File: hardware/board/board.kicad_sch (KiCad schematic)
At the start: 64 parts, among them J1 Power, J10 OUT B3, J12 IN C, J13 OUT C1, J14 OUT C2, J15 OUT C3, J17 OUT D, J18 IN D1, J19 IN D2, J2 IN A, J20 IN D3, J3 OUT A1, J4 OUT A2, J5 OUT A3, J7 IN B, J8 OUT B1, J9 OUT B2, U1 OPA4991, U2 OPA4991, U4 OPA4991, U6 OPA4991

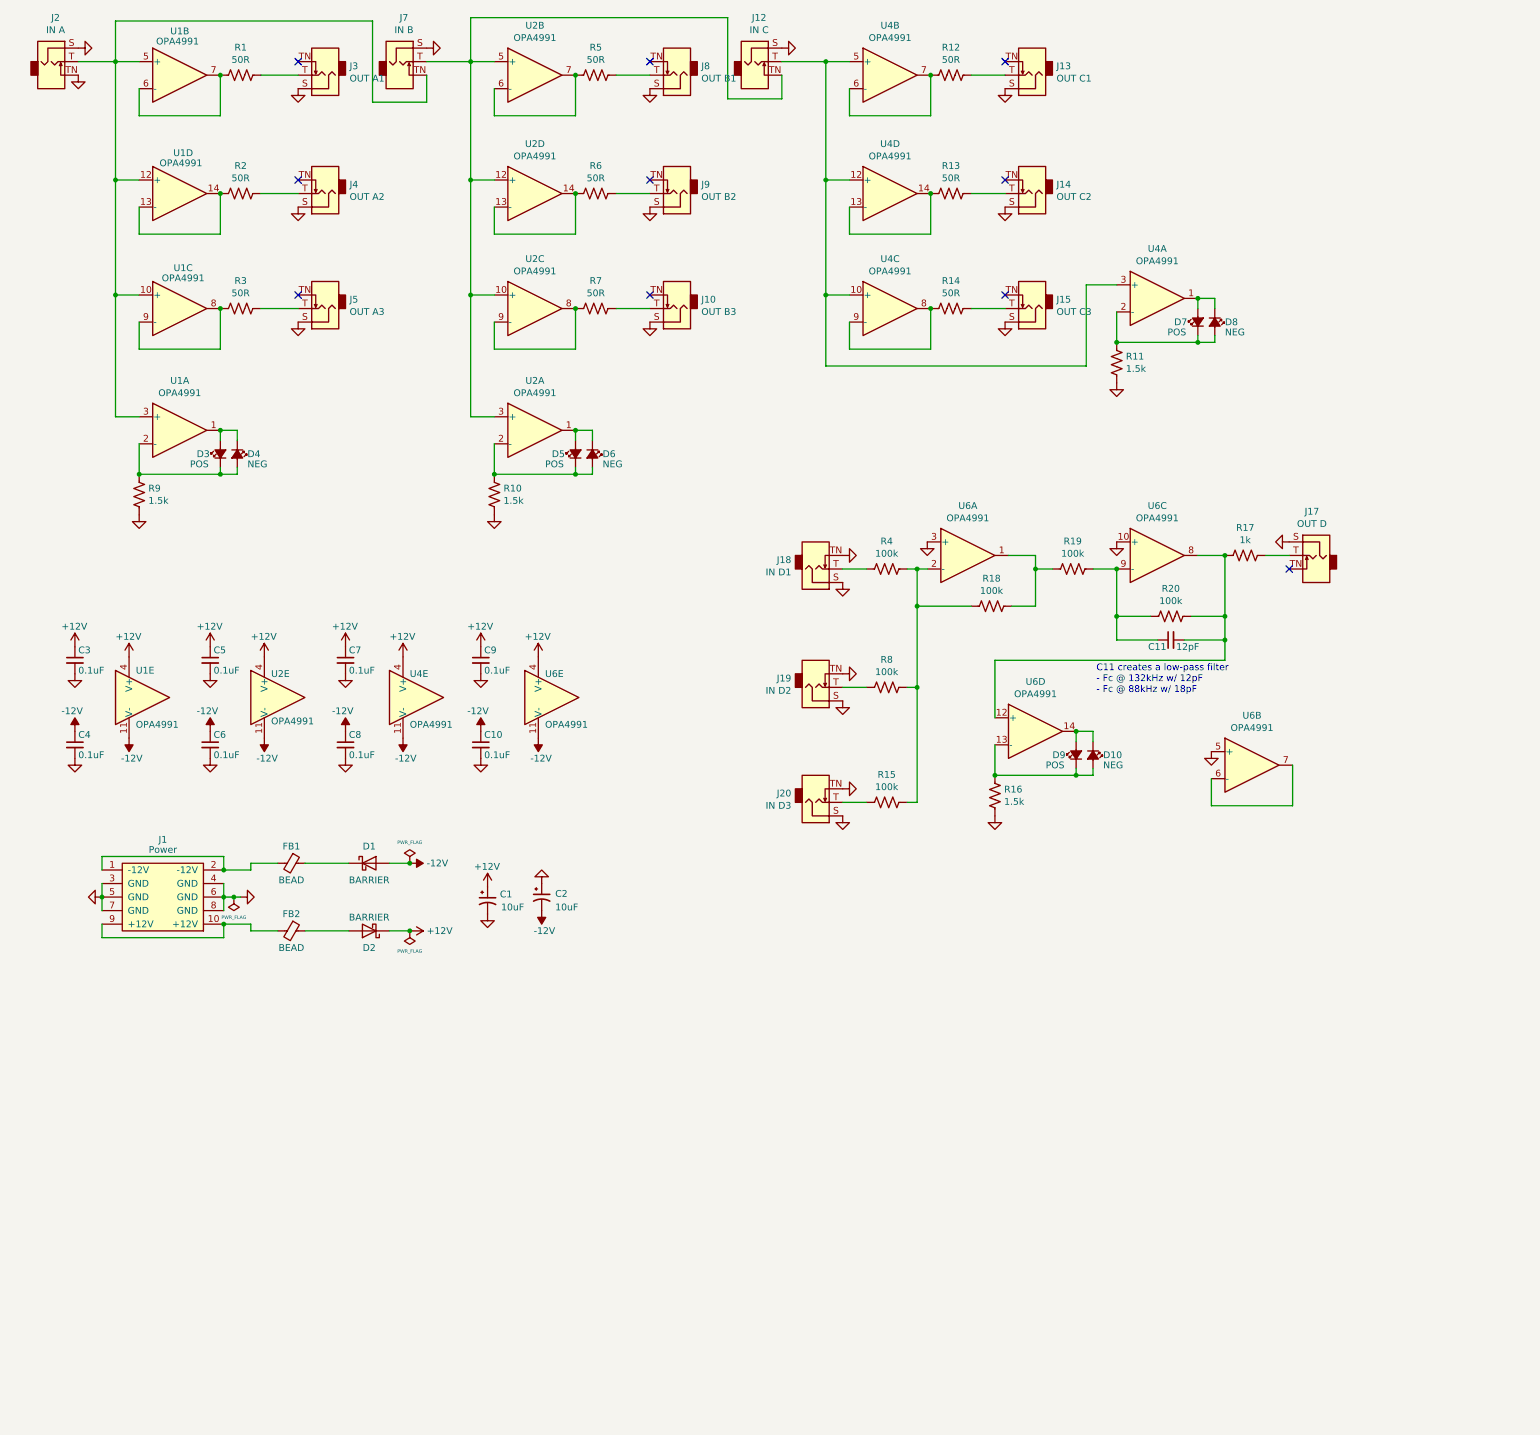
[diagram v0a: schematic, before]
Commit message: hardware: revision 3
- Update to new Winterbloom footprints
- Update to match current Winterbloom design standards
- Re-route traces
- Update legends
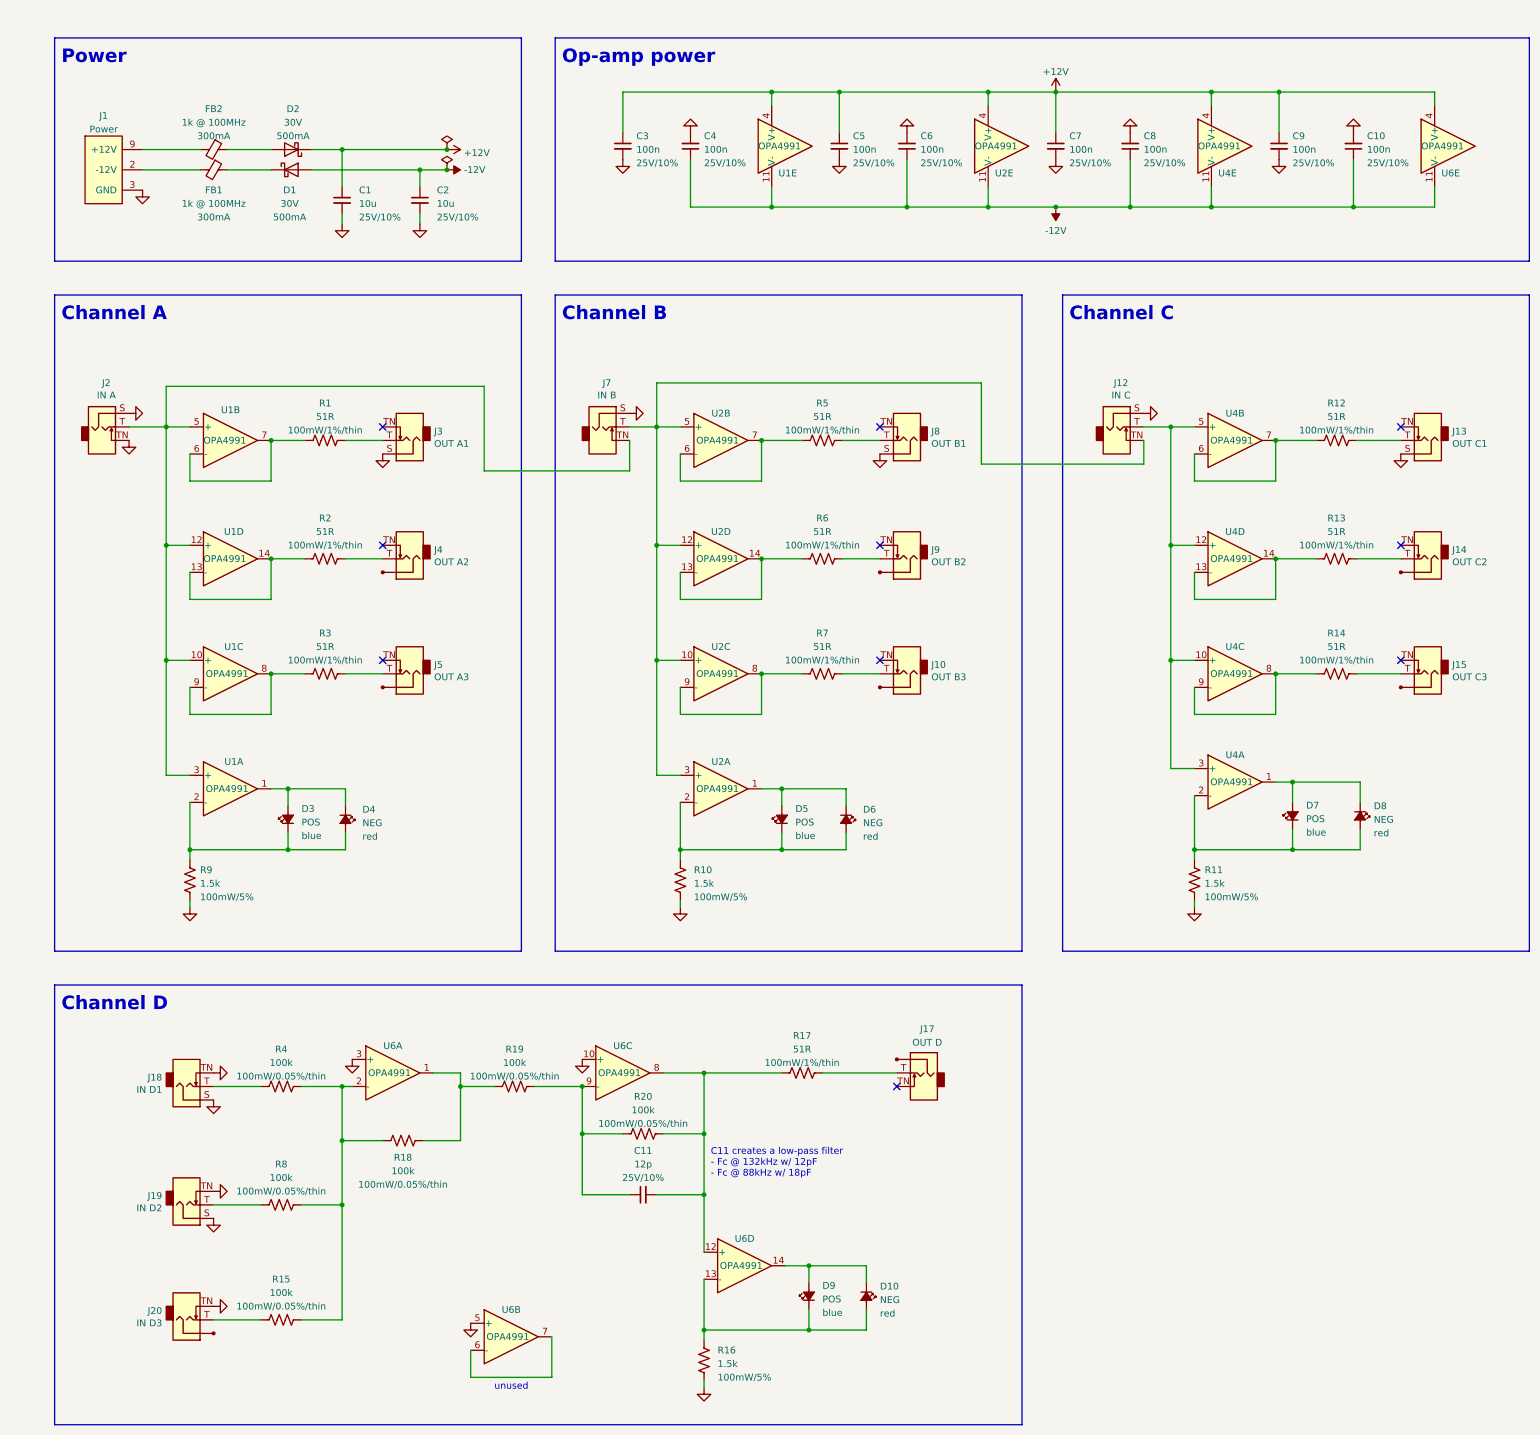
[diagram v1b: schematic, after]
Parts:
- C1, C2: value 10uF -> 10u; footprint Capacitor_SMD:C_0805_2012Metric_Pad1.18x1.45mm_HandSolder -> winterbloom:C_0805_HandSolder; symbol Device:CP1_Small -> Device:C_Small; Rating (none) -> 25V/10%
- C10, C3, C4, C5, C6, C7, C8, C9: value 0.1uF -> 100n; footprint Capacitor_SMD:C_0603_1608Metric_Pad1.08x0.95mm_HandSolder -> winterbloom:C_0603_HandSolder; Rating (none) -> 25V/10%
- C11: value 12pF -> 12p; footprint Capacitor_SMD:C_0603_1608Metric_Pad1.08x0.95mm_HandSolder -> winterbloom:C_0603_HandSolder; Rating (none) -> 25V/10%
- D1, D2: value BARRIER -> 30V; footprint winterbloom:DIODE_SOD-123_SOD-123F -> winterbloom:D_SOD-123+SOD-123F; Rating (none) -> 500mA
- D10, D4, D6, D8: symbol Device:LED_Small_ALT -> Device:LED_Small_Filled; Rating (none) -> red
- D3, D5, D7, D9: symbol Device:LED_Small_ALT -> Device:LED_Small_Filled; Rating (none) -> blue
- FB1, FB2: value BEAD -> 1k @ 100MHz; footprint Inductor_SMD:L_0603_1608Metric_Pad1.05x0.95mm_HandSolder -> winterbloom:L_0603_HandSolder; symbol Device:Ferrite_Bead_Small -> Device:FerriteBead_Small; Notes 300mA -> (none); Rating (none) -> 300mA
- J1: footprint winterbloom:Eurorack_Power -> winterbloom:Eurorack_Power_2x5_Shrouded_Lock; MPN (none) -> 302-S101
- J10, J14, J15, J17, J20, J4, J5, J9: footprint winterbloom:WQP-WQP518MA-skinny -> winterbloom:AudioJack_WQP518MA_No_S; symbol winterbloom:Eurorack_Mono_Jack -> winterbloom:Eurorack_Mono_Jack_No_S; MPN (none) -> WQP-WQP518MA
- J12, J13, J18, J19, J2, J3, J7, J8: footprint winterbloom:WQP-WQP518MA-skinny -> winterbloom:AudioJack_WQP518MA_Compact_S; MPN (none) -> WQP-WQP518MA
- R1, R12, R13, R14, R2, R3, R5, R6, R7: value 50R -> 51R; footprint Resistor_SMD:R_0603_1608Metric_Pad0.98x0.95mm_HandSolder -> winterbloom:R_0603_HandSolder; Rating (none) -> 100mW/1%/thin
- R10, R11, R16, R9: footprint Resistor_SMD:R_0603_1608Metric_Pad0.98x0.95mm_HandSolder -> winterbloom:R_0603_HandSolder; Rating (none) -> 100mW/5%
- R15, R18, R19, R20, R4, R8: footprint Resistor_SMD:R_0603_1608Metric_Pad0.98x0.95mm_HandSolder -> winterbloom:R_0603_HandSolder; Rating (none) -> 100mW/0.05%/thin
- R17: value 1k -> 51R; footprint Resistor_SMD:R_0603_1608Metric_Pad0.98x0.95mm_HandSolder -> winterbloom:R_0603_HandSolder; Notes 1%, thin film -> thin film, highest possible wattage for size; Rating (none) -> 100mW/1%/thin; mpn ERA-3AED102V -> (none)
- U1, U2, U4, U6: symbol winterbloom:OPA4197 -> winterbloom:OPA4991
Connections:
- net -12V: now also C2.1; no longer C2.2
- net GND: now also C2.2; no longer C2.1, J10.S (Sleeve), J14.S (Sleeve), J15.S (Sleeve), J17.S (Sleeve), J20.S (Sleeve), J4.S (Sleeve), J5.S (Sleeve), J9.S (Sleeve)
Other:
- note added: "Channel A"
- note added: "Channel B"
- note added: "Channel C"
- note added: "Channel D"
- note added: "Op-amp power"
- note added: "Power"
- note added: "unused"
- moved on the sheet: C10, C11, C3, C4, C5, C6, C7, C8, C9, D1, D10, D2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

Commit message: hardware: Changes for self-sourcing
- Add manufacturer part numbers and DigiKey, Mouser, and LCSC part numbers for all BOM items.
- Split schematic into multiple US letter-sized sheets.
- Update to new Winterbloom drawing sheet.
- Create new PDF of schematic.
- Create gerbers.zip with pre-made Gerbers.
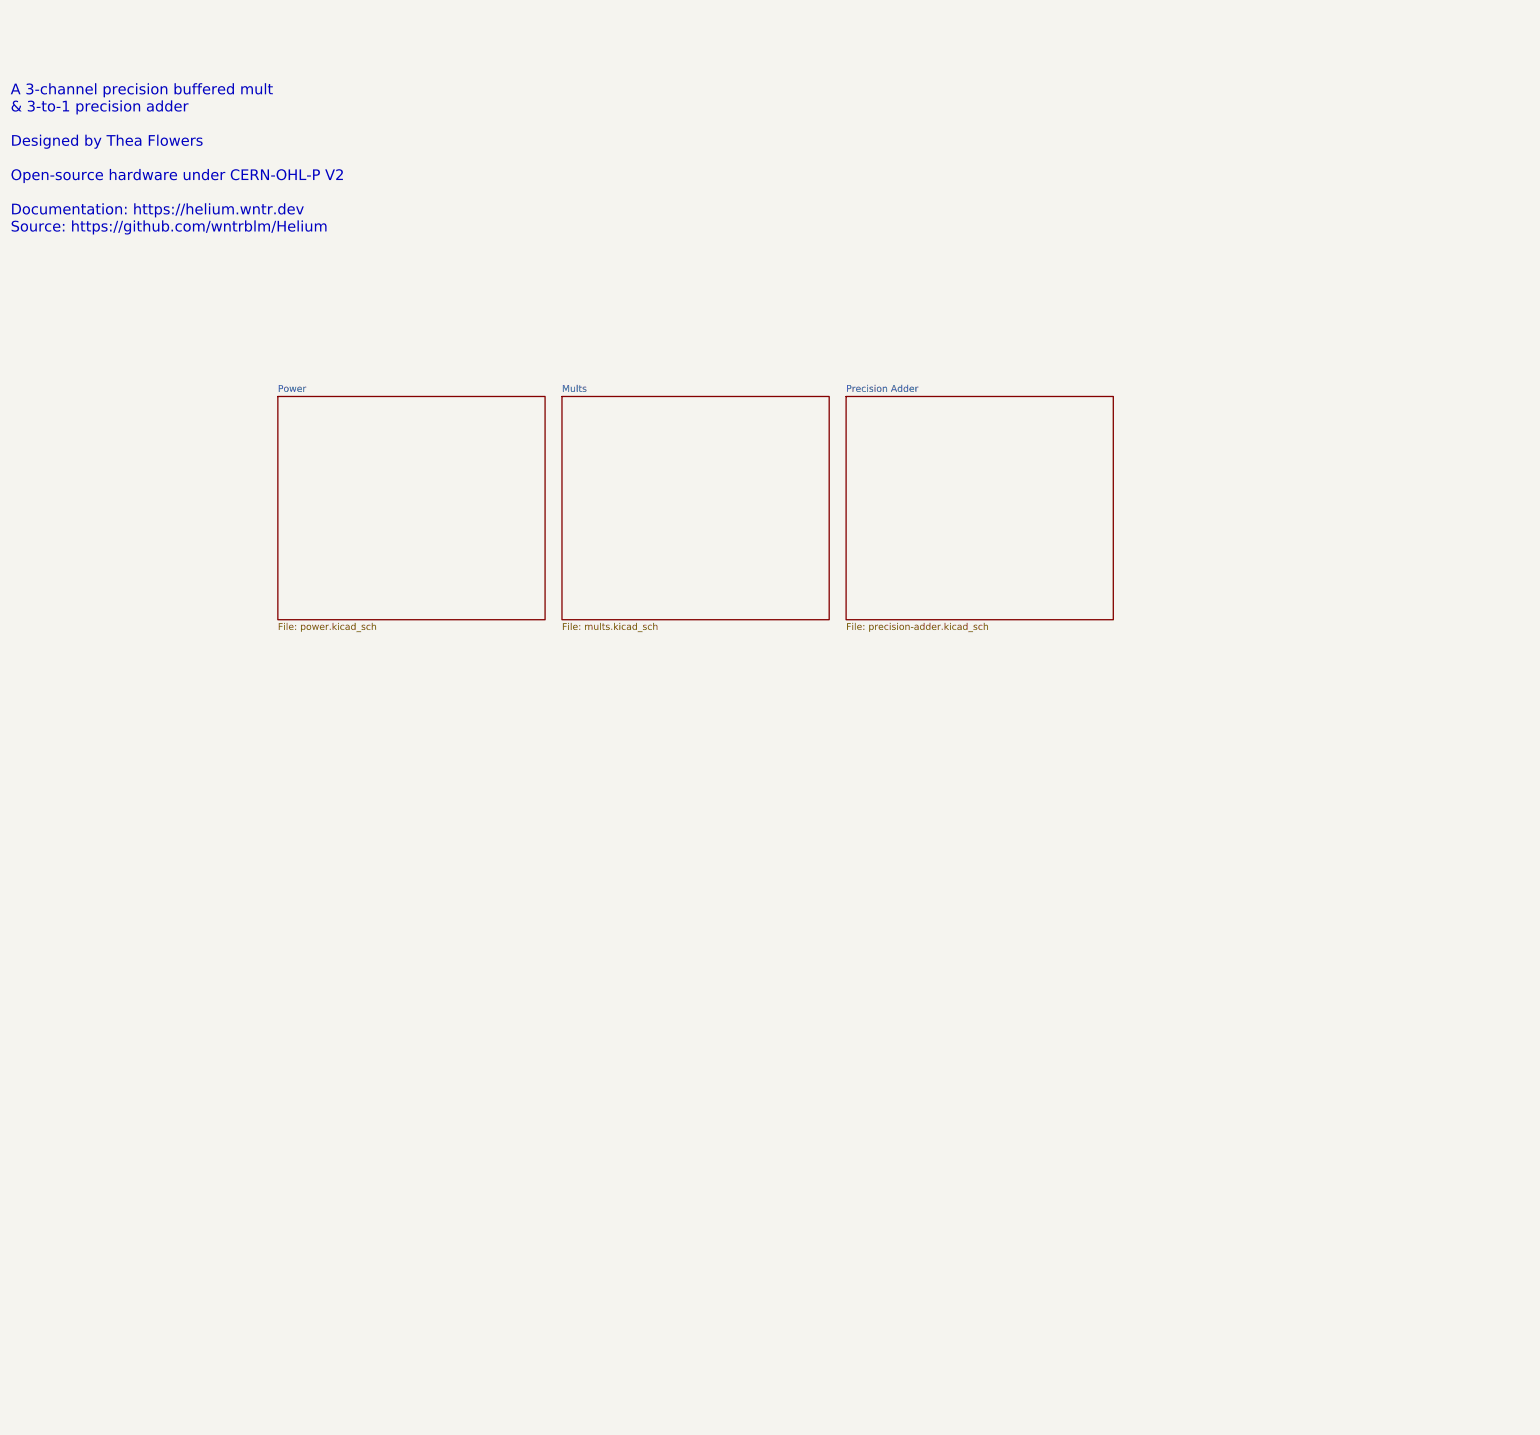
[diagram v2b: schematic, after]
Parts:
- removed C1, C2: 10u, winterbloom:C_0805_HandSolder, symbol Device:C_Small
- removed C10, C3, C4, C5, C6, C7, C8, C9: 100n, winterbloom:C_0603_HandSolder, symbol Device:C_Small
- removed C11: 12p, winterbloom:C_0603_HandSolder, symbol Device:C_Small
- removed D1, D2: 30V, winterbloom:D_SOD-123+SOD-123F, symbol Diode:1N5819
- removed D10, D4, D6, D8: NEG, winterbloom:LED_0805_Kingbright_APT2012, symbol Device:LED_Small_Filled
- removed D3, D5, D7, D9: POS, winterbloom:LED_0805_Kingbright_APT2012, symbol Device:LED_Small_Filled
- removed FB1, FB2: 1k @ 100MHz, winterbloom:L_0603_HandSolder, symbol Device:FerriteBead_Small
- removed J1: Power, winterbloom:Eurorack_Power_2x5_Shrouded_Lock, symbol winterbloom:Eurorack_Power
- removed J10: OUT B3, winterbloom:AudioJack_WQP518MA_No_S, symbol winterbloom:Eurorack_Mono_Jack_No_S
- removed J12: IN C, winterbloom:AudioJack_WQP518MA_Compact_S, symbol winterbloom:Eurorack_Mono_Jack
- removed J13: OUT C1, winterbloom:AudioJack_WQP518MA_Compact_S, symbol winterbloom:Eurorack_Mono_Jack
- removed J14: OUT C2, winterbloom:AudioJack_WQP518MA_No_S, symbol winterbloom:Eurorack_Mono_Jack_No_S
- removed J15: OUT C3, winterbloom:AudioJack_WQP518MA_No_S, symbol winterbloom:Eurorack_Mono_Jack_No_S
- removed J17: OUT D, winterbloom:AudioJack_WQP518MA_No_S, symbol winterbloom:Eurorack_Mono_Jack_No_S
- removed J18: IN D1, winterbloom:AudioJack_WQP518MA_Compact_S, symbol winterbloom:Eurorack_Mono_Jack
- removed J19: IN D2, winterbloom:AudioJack_WQP518MA_Compact_S, symbol winterbloom:Eurorack_Mono_Jack
- removed J2: IN A, winterbloom:AudioJack_WQP518MA_Compact_S, symbol winterbloom:Eurorack_Mono_Jack
- removed J20: IN D3, winterbloom:AudioJack_WQP518MA_No_S, symbol winterbloom:Eurorack_Mono_Jack_No_S
- removed J3: OUT A1, winterbloom:AudioJack_WQP518MA_Compact_S, symbol winterbloom:Eurorack_Mono_Jack
- removed J4: OUT A2, winterbloom:AudioJack_WQP518MA_No_S, symbol winterbloom:Eurorack_Mono_Jack_No_S
- removed J5: OUT A3, winterbloom:AudioJack_WQP518MA_No_S, symbol winterbloom:Eurorack_Mono_Jack_No_S
- removed J7: IN B, winterbloom:AudioJack_WQP518MA_Compact_S, symbol winterbloom:Eurorack_Mono_Jack
- removed J8: OUT B1, winterbloom:AudioJack_WQP518MA_Compact_S, symbol winterbloom:Eurorack_Mono_Jack
- removed J9: OUT B2, winterbloom:AudioJack_WQP518MA_No_S, symbol winterbloom:Eurorack_Mono_Jack_No_S
- removed R1, R12, R13, R14, R17, R2, R3, R5, R6, R7: 51R, winterbloom:R_0603_HandSolder, symbol Device:R_US
- removed R10, R11, R16, R9: 1.5k, winterbloom:R_0603_HandSolder, symbol Device:R_US
- removed R15, R18, R19, R20, R4, R8: 100k, winterbloom:R_0603_HandSolder, symbol Device:R_US
- removed U1, U2, U4, U6: OPA4991, Package_SO:TSSOP-14_4.4x5mm_P0.65mm, symbol winterbloom:OPA4991
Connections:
- no-connect marks 10 -> 0
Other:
- added sheet Mults (mults.kicad_sch)
- added sheet Power (power.kicad_sch)
- added sheet Precision Adder (precision-adder.kicad_sch)
- note added: "A 3-channel precision buffered mult & 3-to-1 precision adder Designed by Thea Flowers Open-source hardware under CERN-OHL-P V2 Documentation: https://helium.wntr.dev Source: https://github.com/wntrblm/Helium"
- note removed: "C11 creates a low-pass filter - Fc @ 132kHz w/ 12pF - Fc @ 88kHz w/ 18pF"
- note removed: "Channel A"
- note removed: "Channel B"
- note removed: "Channel C"
- note removed: "Channel D"
- note removed: "Op-amp power"
- note removed: "Power"
- note removed: "unused"
